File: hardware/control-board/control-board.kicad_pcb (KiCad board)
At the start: 4 copper layers, 100 x 100 mm, 233 parts, among them J1 XH-2A, J10 XH-2A, J11 XH-2A, J12 XH-2A, J13 XH-2A, J14 XH-2A, J15 XH-2A, J16 XH-2A, J17 XH-2A, J18 XH-2A, J19 XH-2A, J2 XH-2A, J20 XH-2A, J21 XH-2A, J22 XH-4A, J23 XH-4A, J24 XH-4A, J25 XH-4A, J26 XH-4A, J27 XH-4A, J28 XH-4A, J29 XH-2A, J3 XH-2A, J30 XH-2A, J31 XH-2A, J32 XH-2A, J33 XH-2A, J34 XH-2A, J35 XH-2A, J36 XH-2A, J37 XH-4A, J38 HB9500M-9.5-2P, J4 XH-2A, J5 XH-2A, J6 XH-2A, J7 XH-2A, J8 XH-2A, J9 XH-2A, Q1 AO3400A, Q10 AO3400A, Q11 AO3400A, Q12 AO3400A, Q2 AO3400A, Q3 AO3400A, Q4 AO3400A, Q5 AO3400A, Q6 AO3400A, Q7 AO3400A, Q8 AO3400A, Q9 AO3400A, SW1 TS-1187A-B-A-B, SW2 TS-1187A-B-A-B, T1 HX1188NL, U1 STM32H723ZGTx, U2 DP83825I, U3 TMC2209-LA, U4 TMC2209-LA, U5 XL1509-5.0, U6 AMS1117-3.3, U7 SN74LVC4245APWR, U8 W25Q128JVS, U9 TMI8340_C2985071, X1 X322525MOB4SI, X2 X322525MOB4SI, X3 Q13FC1350000400

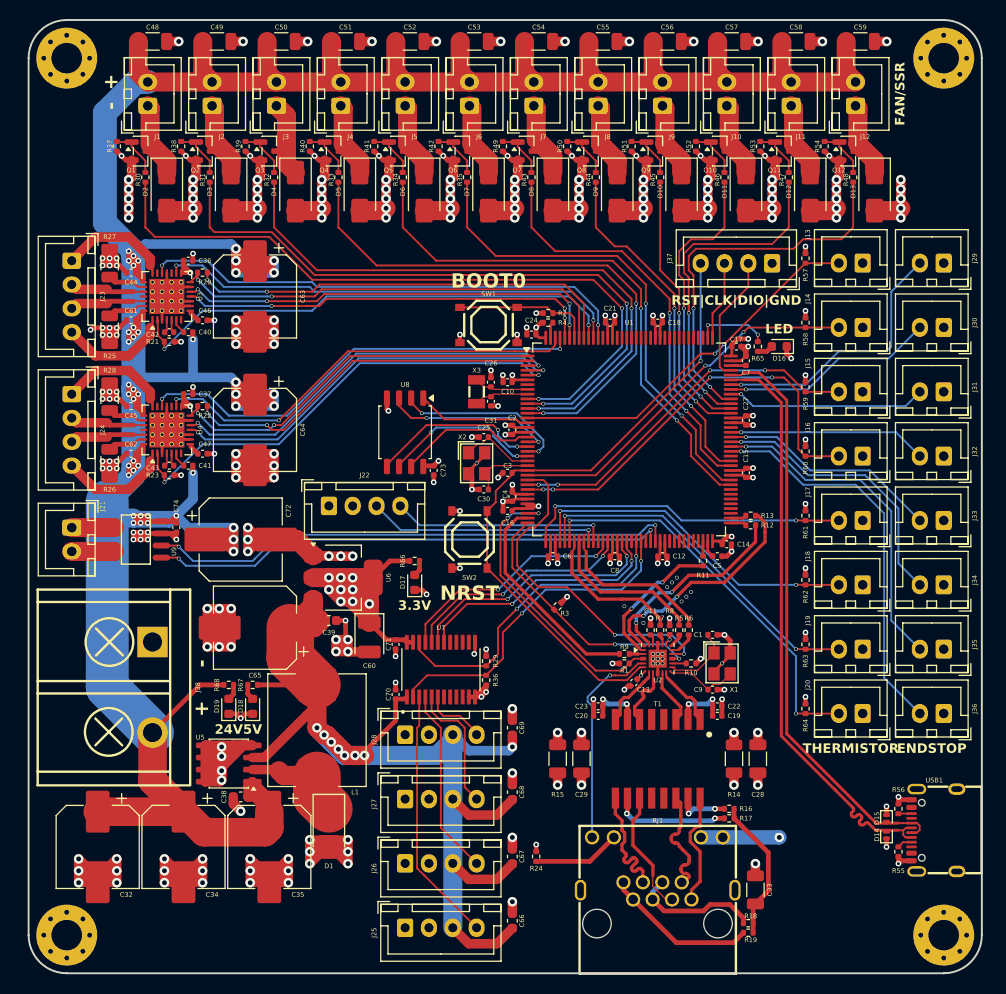
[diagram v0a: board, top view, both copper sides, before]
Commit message: added indicator I/O, text labels
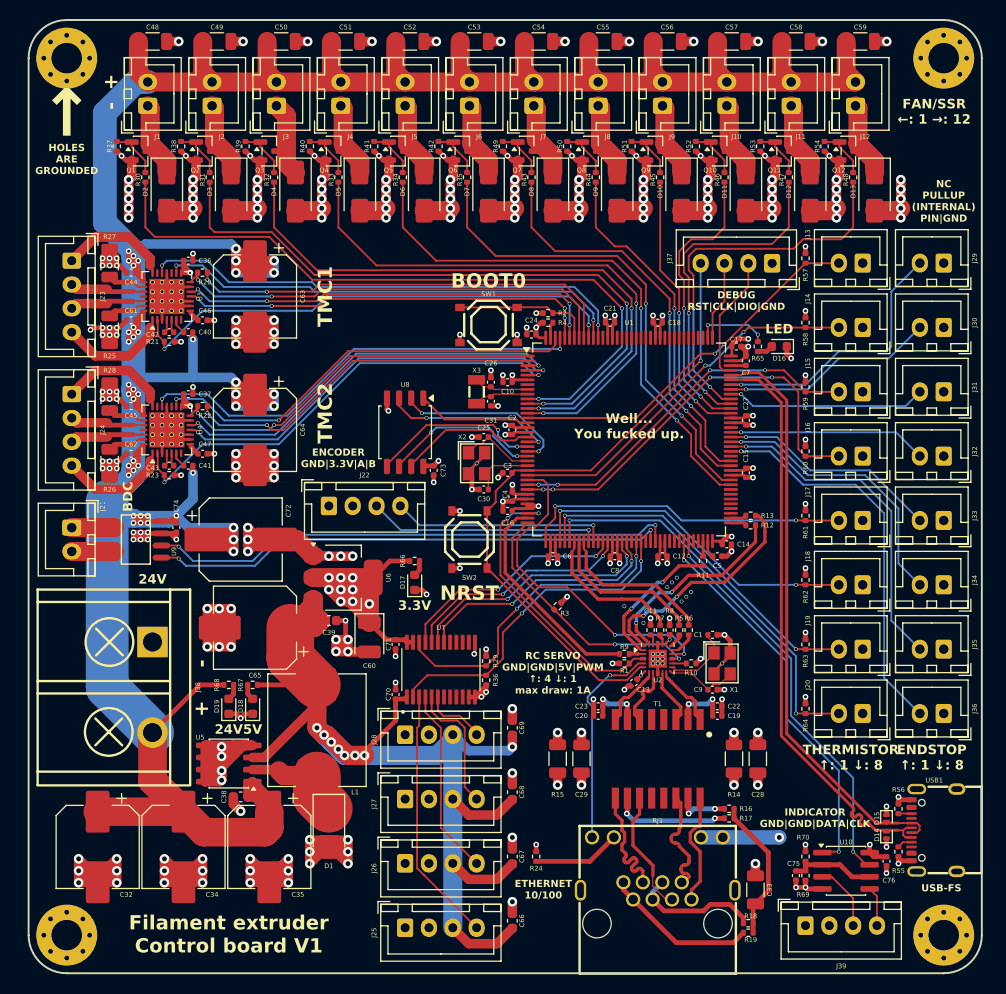
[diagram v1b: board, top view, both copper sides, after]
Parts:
- added C75: 100nF 50V, Capacitor_SMD:C_0402_1005Metric, F.Cu at (30.5, 39.8)
- added C76: 100nF 50V, Capacitor_SMD:C_0402_1005Metric, F.Cu at (40.0, 38.2)
- added J39: XH-4A, Connector_JST:JST_XH_B4B-XH-A_1x04_P2.50mm_Vertical, F.Cu at (31.5, 45.0)
- added R69: 10kR 1%, Resistor_SMD:R_0402_1005Metric, F.Cu at (31.5, 39.8)
- added R70: 33kR 1%, Resistor_SMD:R_0402_1005Metric, F.Cu at (31.5, 37.8)
- added U10: LM393, Package_SO:SOIC-8_3.9x4.9mm_P1.27mm, F.Cu at (35.8, 39.2)
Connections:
- U1 pad 66: unconnected-(U1-PE13-Pad66) -> /INDICATOR_DATA
- U1 pad 67: unconnected-(U1-PE14-Pad67) -> /INDICATOR_CLK
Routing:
- net /INDICATOR_CLK: track 0.00 -> 42.0 mm, vias 0 -> 2
- net /INDICATOR_DATA: track 0.00 -> 41.2 mm, vias 0 -> 2
- net /INDICATOR_VREF: track 0.00 -> 9.30 mm
- net /INDICATOR_DATA_IN: track 0.00 -> 7.02 mm
- net GND: track 582.7 -> 587.8 mm, vias 255 -> 258
- net /INDICATOR_CLK_IN: track 0.00 -> 4.17 mm
- net +3.3V: track 106.3 -> 109.9 mm, vias 43 -> 45
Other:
- board text added: "BDC"
- board text added: "DEBUG RST|CLK|DIO|GND"
- board text added: "ENCODER GND|3.3V|A|B"
- board text added: "ENDSTOP ↑: 1 ↓: 8"
- board text added: "ETHERNET 10/100"
- board text added: "FAN/SSR ←: 1 →: 12"
- board text added: "Filament extruder Control board V1"
- board text added: "HOLES ARE GROUNDED"
- board text added: "INDICATOR GND|GND|DATA|CLK"
- board text added: "NC PULLUP (INTERNAL) PIN|GND"
- board text added: "RC SERVO GND|GND|5V|PWM ↑: 4 ↓: 1 max draw: 1A"
- board text added: "THERMISTOR ↑: 1 ↓: 8"
- board text added: "TMC1"
- board text added: "TMC2"
- board text added: "USB-FS"
- board text added: "Well... You fucked up."
- board text added: "↑"
- board text removed: "ENDSTOP"
- board text removed: "FAN/SSR"
- board text removed: "RST|CLK|DIO|GND"
- board text removed: "THERMISTOR"

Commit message: changed ethernet termination capacitors to 1nF
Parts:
- C28, C29: value 4.7nF 2kV -> 1nF 2kV
- C33: value 10nF 2kV -> 1nF 2kV
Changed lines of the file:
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@@
 			)
 		)
-		(property "Value" "4.7nF 2kV"
+		(property "Value" "1nF 2kV"
 			(at 0 1.850001 270)
 			(unlocked yes)
@@
 			)
 		)
-		(property "Value" "4.7nF 2kV"
+		(property "Value" "1nF 2kV"
 			(at 0 1.850001 270)
 			(unlocked yes)
@@
 			)
 		)
-		(property "Value" "10nF 2kV"
+		(property "Value" "1nF 2kV"
 			(at 0 1.850001 90)
 			(unlocked yes)
